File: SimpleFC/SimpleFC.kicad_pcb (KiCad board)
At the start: 4 copper layers, 50 x 50 mm, 127 parts, among them J1 M02, J11 M04, J12 USB, J13 M04, J14 M03, J2 TF_SDIO, J3 M04, J4 M04, J5 M10, J6 M10, J7 M10, J8 UFL, Q1 AO3407A, U1 STM32F405RGTx, U10 74LVC1G86, U11 TJA1050, U12 NEO-M8, U13 TPS79333, U2 MAG3110, U3 ICM-20689, U4 MS5611, U5 MP2403, U6 SPX3819, U7 AT24C512C, U8 74LVC1G86, U9 SN74LVC245APW, X1 25Mhz

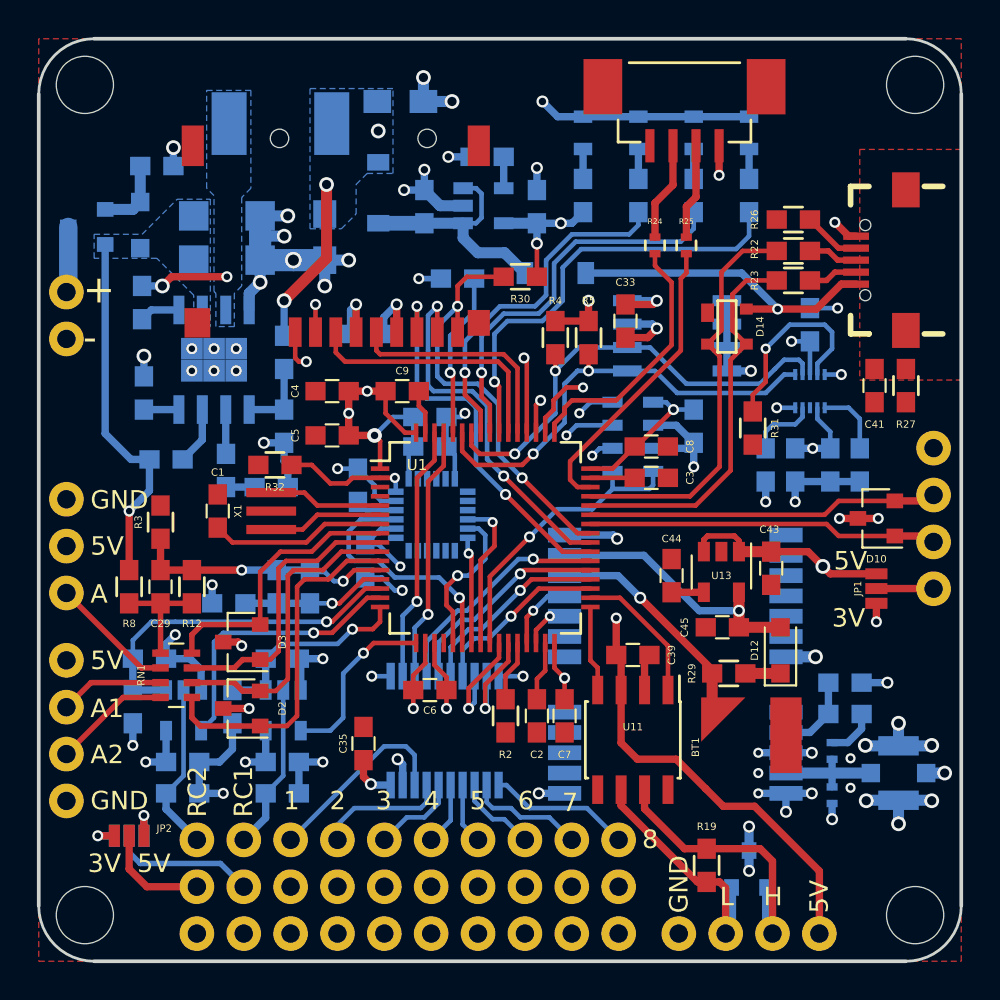
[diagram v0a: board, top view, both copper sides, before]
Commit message: Refactor SimpleFC schematics with latest KiCAD libraries.
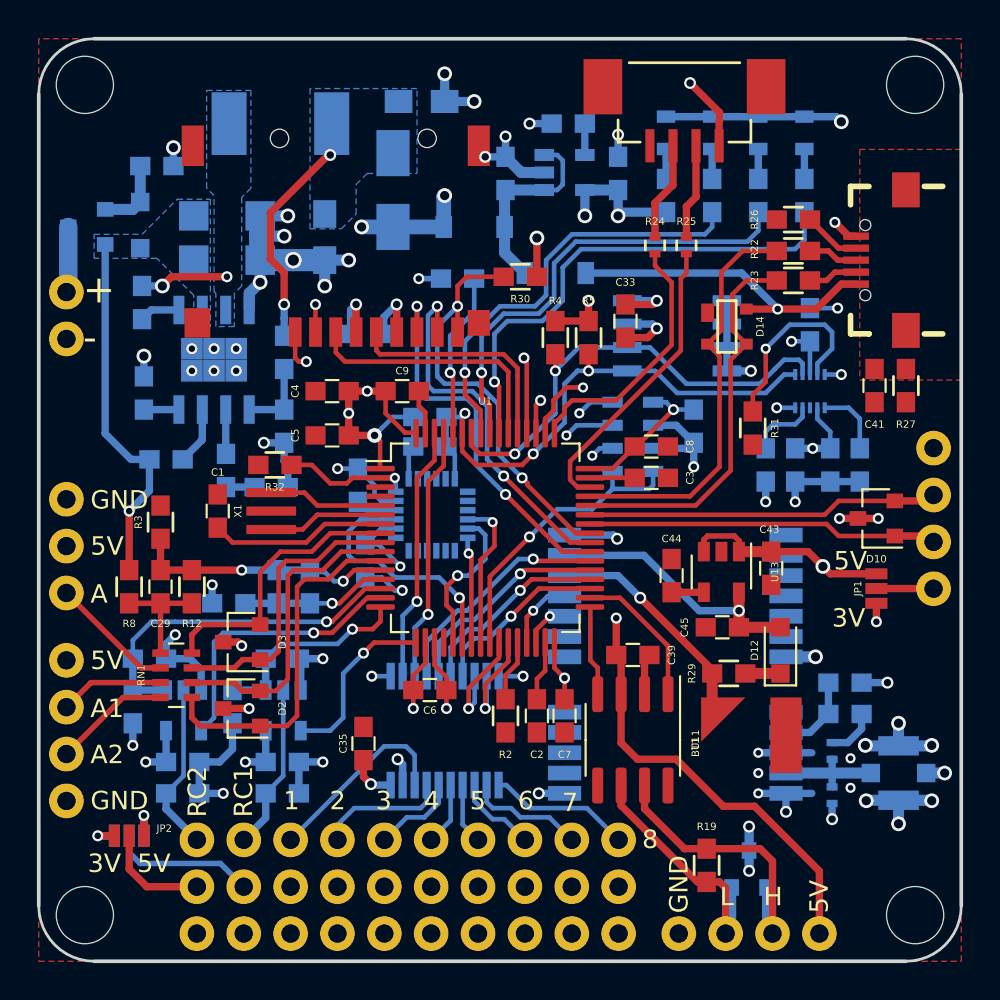
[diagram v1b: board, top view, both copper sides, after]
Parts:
- added D15: 3A, STD_SMD:D_SMA_Standard, B.Cu at (144.2, 83.2)
- U11: footprint STD_SMD:SOIC-8_3.9x4.9mm_Pitch1.27mm -> Package_SO:SOIC-8_3.9x4.9mm_P1.27mm
- U12: value NEO-M8 -> NEO-M8N
- U13: value TPS79333 -> TPS79333-EP; footprint STD_SMD:SOT-23-5 -> Package_TO_SOT_SMD:SOT-23-5
- U6: value SPX3819 -> SPX3819M5-L-3-3; footprint STD_SMD:SOT-23-5 -> Package_TO_SOT_SMD:SOT-23-5
- U9: footprint Package_SSOP:TSSOP-20_4.4x6.5mm_P0.65mm -> Package_SO:TSSOP-20_4.4x6.5mm_P0.65mm
- moved D4 5.52 mm to (148.6, 85.2), turned to 180 degrees
- moved C30 4.75 mm to (156.4, 82.3)
- moved C31 4.75 mm to (150.3, 82.3)
- moved U6 4.75 mm to (153.5, 82.2)
- moved C32 4.75 mm to (153.7, 79.6)
- moved D6 4.50 mm to (159.0, 80.1)
- moved R13 4.50 mm to (159.0, 83.5)
- moved D9 4.00 mm to (161.5, 80.1)
- moved R16 4.00 mm to (161.5, 83.5)
- moved D8 3.50 mm to (164.0, 80.1)
- moved R15 3.50 mm to (164.0, 83.5)
- moved D7 3.00 mm to (166.5, 80.1)
- moved R14 3.00 mm to (166.5, 83.5)
- moved C28 1.15 mm to (145.8, 78.4)
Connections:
- net ADC1_IN10 renamed /A0
- net ADC1_IN11 renamed /A1
- net ADC1_IN12 renamed /A2
- net ADC1_IN13 renamed /A3
- net ADC_CURR renamed /Connectors/ADC_CURR
- net ADC_IN2 renamed /Connectors/ADC_IN2
- net ADC_IN3 renamed /Connectors/ADC_IN3
- net BARO_CS renamed /BARO_CS
- net CAN2_RX renamed /STM32F4/CAN2_RX
- net CAN2_TX renamed /STM32F4/CAN2_TX
- net CANH renamed /Connectors/CANH
- net CANL renamed /Connectors/CANL
- net DBG_LED renamed /STM32F4/DBG_LED
- net GPS_LED renamed /STM32F4/GPS_LED
- net I2C1_SCL renamed /IMU/I2C1_SCL
- net I2C1_SDA renamed /IMU/I2C1_SDA
- net M1 renamed /M1
- net M2 renamed /M2
- net M3 renamed /M3
- net M4 renamed /M4
- net M5 renamed /M5
- net M6 renamed /M6
- net M7 renamed /M7
- net M8 renamed /M8
- net MAG_INT renamed /IMU/MAG_INT
- net MPU_CS renamed /MPU_CS
- net MPU_INT renamed /MPU_INT
- net RC_IN1 renamed /Connectors/RC_IN1
- net RC_IN2 renamed /Connectors/RC_IN2
- net RDY_LED renamed /STM32F4/RDY_LED
- net SDIO_CK renamed /CK
- net SDIO_CMD renamed /CMD
- net SDIO_D0 renamed /D0
- net SDIO_D1 renamed /D1
- net SDIO_D2 renamed /D2
- net SDIO_D3 renamed /D3
- net SD_DECT renamed /DECT
- net SPI1_MISO renamed /MISO
- net SPI1_MOSI renamed /MOSI
- net SPI1_SCK renamed /SCK
- net SWCLK renamed /Connectors/SWCLK
- net SWDIO renamed /Connectors/SWDIO
- net T12C1 renamed /PWM6
- net T12C2 renamed /PWM5
- net T3C1 renamed /PWM4
- net T3C2 renamed /PWM3
- net T3C3 renamed /PWM7
- net T3C4 renamed /PWM8
- net T4C3 renamed /PWM2
- net T4C4 renamed /PWM1
- net U1RX renamed /Connectors/U1RX
- net U1TX renamed /Connectors/U1TX
- net U2RX renamed /STM32F4/U2RX
- net U2TX renamed /STM32F4/U2TX
- net U3RX renamed /IMU/U3RX
- net U3TX renamed /IMU/U3TX
- net U4RX renamed /STM32F4/U4RX
- net U4TX renamed /STM32F4/U4TX
- net USBDM renamed /Connectors/USBDM
- net USBDP renamed /Connectors/USBDP
- net V_SW renamed /Power/V_SW
- C27 pad 1: +5V -> /Power/PRE5V
- C28 pad 1: +5V -> /Power/PRE5V
- J6 pad 10: Net-(J6-Pad10) -> (no net)
- J6 pad 3: Net-(J6-Pad3) -> (no net)
- J6 pad 4: Net-(J6-Pad4) -> (no net)
- J6 pad 5: Net-(J6-Pad5) -> (no net)
- J6 pad 6: Net-(J6-Pad6) -> (no net)
- J6 pad 7: Net-(J6-Pad7) -> (no net)
- J6 pad 8: Net-(J6-Pad8) -> (no net)
- J6 pad 9: Net-(J6-Pad9) -> (no net)
- L2 pad 2: +5V -> /Power/PRE5V
- R7 pad 1: +5V -> /Power/PRE5V
- U2 pad 3: Net-(U2-Pad3) -> (no net)
- U3 pad 1: Net-(U3-Pad1) -> (no net)
- U3 pad 14: Net-(U3-Pad14) -> (no net)
- U3 pad 15: Net-(U3-Pad15) -> (no net)
- U3 pad 16: Net-(U3-Pad16) -> (no net)
- U3 pad 17: Net-(U3-Pad17) -> (no net)
- U3 pad 19: Net-(U3-Pad19) -> (no net)
- U3 pad 2: Net-(U3-Pad2) -> (no net)
- U3 pad 20: Net-(U3-Pad20) -> (no net)
- U3 pad 21: Net-(U3-Pad21) -> (no net)
- U3 pad 3: Net-(U3-Pad3) -> (no net)
- U3 pad 4: Net-(U3-Pad4) -> (no net)
- U3 pad 5: Net-(U3-Pad5) -> (no net)
- U3 pad 6: Net-(U3-Pad6) -> (no net)
- U3 pad 7: Net-(U3-Pad7) -> (no net)
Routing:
- net /Power/PRE5V: track 0.00 -> 11.5 mm, vias 0 -> 2
- net +5V: track 152.2 -> 157.3 mm, vias 6 -> 5
- net +3V3: track 75.4 -> 79.8 mm, vias 22 -> 23
- net /STM32F4/DBG_LED: track 19.1 -> 23.2 mm
- net /STM32F4/RDY_LED: track 21.4 -> 24.9 mm
- net /STM32F4/GPS_LED: track 23.8 -> 26.9 mm
- net Net-(C31-Pad1): track 13.1 -> 10.6 mm
- net GND: track 145.4 -> 143.7 mm, vias 70 -> 68
- net /Connectors/SWDIO: track 16.1 -> 15.4 mm
- net /IMU/I2C1_SCL: track 25.6 -> 24.9 mm
- net /STM32F4/U4RX: track 15.1 -> 14.4 mm
- added copper zone on B.Cu, net /Power/PRE5V
- removed copper zone on B.Cu, net +5V
